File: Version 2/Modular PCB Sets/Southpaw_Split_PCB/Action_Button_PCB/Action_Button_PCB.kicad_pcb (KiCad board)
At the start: 2 copper layers, 133 x 112 mm, 28 parts, among them J1 Conn_01x06_Socket, J4 Conn_01x07_Socket, J5 Conn_01x07_Socket, X1 SW_SPST, Y1 SW_SPST

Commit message: general part layout
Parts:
- removed J4, J5: Conn_01x07_Socket, Connector_JST:JST_PH_B7B-PH-K_1x07_P2.00mm_Vertical
- removed R10, R11, R9: R, Resistor_THT:R_Axial_DIN0207_L6.3mm_D2.5mm_P10.16mm_Horizontal
- added J2: Conn_01x07_Socket, Connector_JST:JST_PH_B7B-PH-K_1x07_P2.00mm_Vertical, B.Cu at (176.0, 41.0)
- added J3: Conn_01x07_Socket, Connector_JST:JST_PH_B7B-PH-K_1x07_P2.00mm_Vertical, B.Cu at (63.0, 41.0)
- added R2: R, Resistor_THT:R_Axial_DIN0207_L6.3mm_D2.5mm_P10.16mm_Horizontal, F.Cu at (125.4, 83.0)
- added R3: R, Resistor_THT:R_Axial_DIN0207_L6.3mm_D2.5mm_P10.16mm_Horizontal, F.Cu at (97.8, 85.0)
- added R4: R, Resistor_THT:R_Axial_DIN0207_L6.3mm_D2.5mm_P10.16mm_Horizontal, F.Cu at (67.4, 93.0)
- moved D4 101.3 mm to (61.0, 92.0)
- moved D5 101.3 mm to (155.0, 53.0)
- moved D8 100.0 mm to (58.5, 56.0)
- moved R8 96.1 mm to (64.8, 57.0)
- moved D1 73.2 mm to (153.0, 87.0)
- moved D2 65.8 mm to (119.0, 82.0)
- moved R7 51.9 mm to (96.9, 49.0)
- moved D3 48.6 mm to (91.5, 84.0)
- moved R6 48.6 mm to (126.9, 46.0)
- moved D6 48.6 mm to (120.5, 45.0)
- moved R5 46.4 mm to (161.4, 53.0)
- moved D7 44.7 mm to (90.5, 48.0)
- moved J1 9.22 mm to (176.0, 105.0), turned to 90 degrees
- moved R1 1.08 mm to (158.9, 88.0)
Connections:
- D1 pad 1: RB -> A
- D2 pad 1: LB -> B
- D3 pad 1: Y -> RT
- D4 pad 1: X -> LT
- D5 pad 1: LT -> X
- D6 pad 1: RT -> Y
- D7 pad 1: B -> RB
- D8 pad 1: A -> LB
- R1 pad 1: Net-(D8-A) -> Net-(D1-A)
- R5 pad 1: Net-(D7-A) -> Net-(D5-A)
- R7 pad 1: Net-(D5-A) -> Net-(D7-A)
- R8 pad 1: Net-(D4-A) -> Net-(D8-A)
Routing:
- net /Gnd: track 351.0 -> 0.00 mm
- net /3V3: track 240.5 -> 0.00 mm
- net GND: track 238.2 -> 0.00 mm
- net 3v3: track 236.1 -> 0.00 mm
- net /Rotary_Encoder_DT: track 153.1 -> 0.00 mm, vias 2 -> 0
- net LB: track 149.7 -> 0.00 mm, vias 1 -> 0
- net /R3: track 147.1 -> 0.00 mm, vias 2 -> 0
- net /Rotary_Encoder_CLK: track 146.2 -> 0.00 mm, vias 1 -> 0
- net /L3: track 142.6 -> 0.00 mm, vias 2 -> 0
- net /Start: track 136.6 -> 0.00 mm, vias 2 -> 0
- net /Options: track 126.8 -> 0.00 mm, vias 1 -> 0
- net /Guide: track 121.0 -> 0.00 mm, vias 1 -> 0
- net /Right: track 111.6 -> 0.00 mm, vias 2 -> 0
- net RB: track 111.4 -> 0.00 mm
- net /SDA: track 110.3 -> 0.00 mm
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
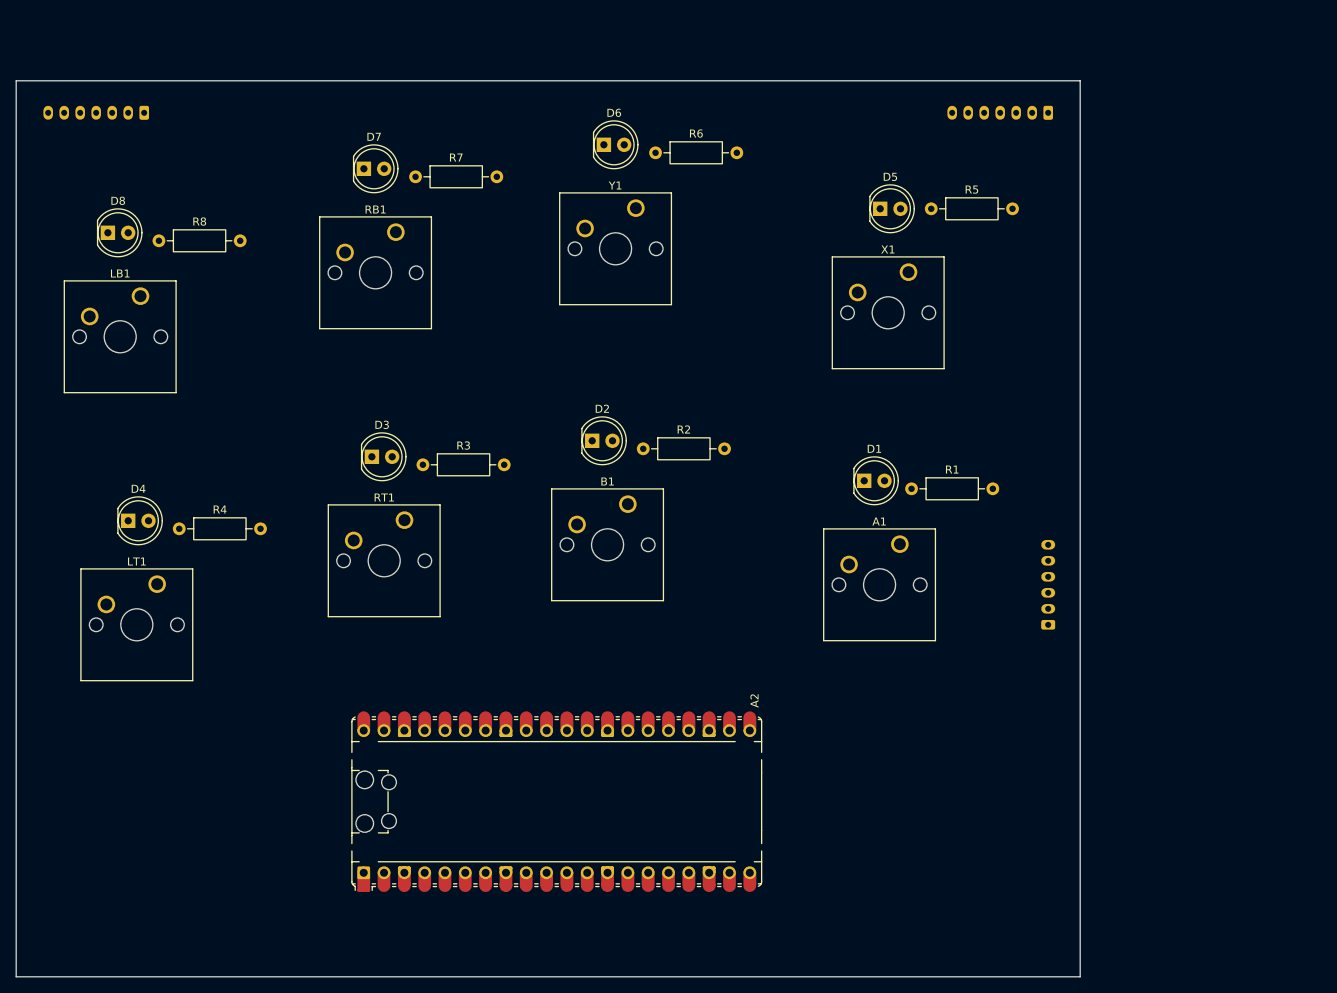
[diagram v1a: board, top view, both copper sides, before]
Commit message: First attempt to use solidworks sketches to align parts in kicad
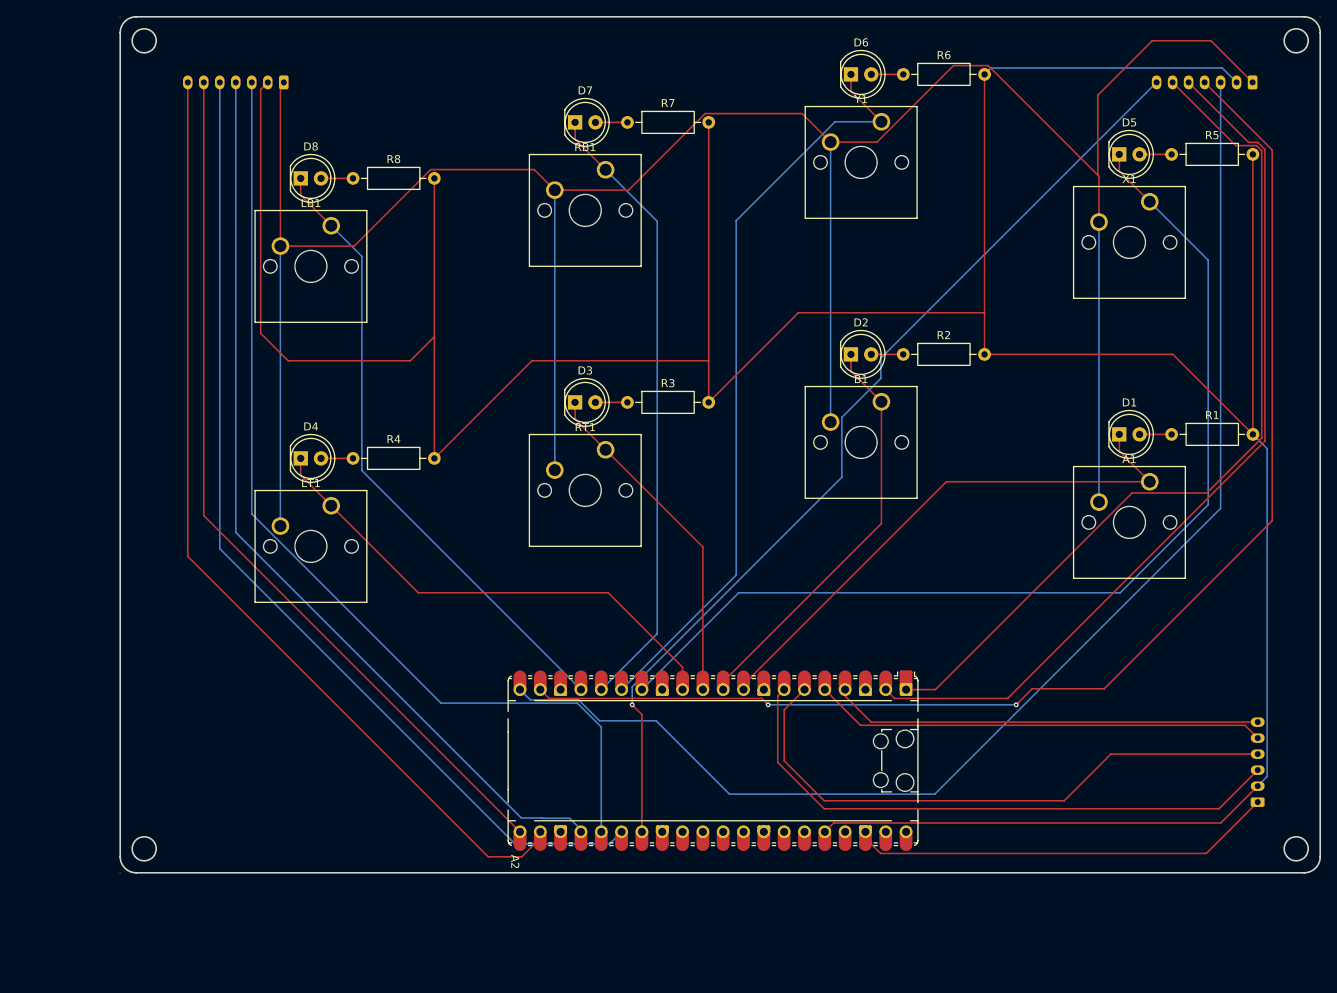
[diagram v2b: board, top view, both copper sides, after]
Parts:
- moved R2 34.6 mm to (157.9, 71.2)
- moved J1 34.3 mm to (202.2, 127.2)
- moved B1 34.2 mm to (155.2, 77.1)
- moved D2 34.1 mm to (151.3, 71.2)
- moved R1 33.2 mm to (191.4, 81.2)
- moved Y1 32.5 mm to (155.2, 42.1)
- moved R6 32.5 mm to (157.9, 36.2)
- moved D1 32.4 mm to (184.9, 81.2)
- moved A1 32.2 mm to (188.7, 87.1)
- moved D6 32.1 mm to (151.3, 36.2)
- moved X1 31.4 mm to (188.7, 52.1)
- moved R5 30.8 mm to (191.4, 46.2)
- moved D5 30.6 mm to (184.9, 46.2)
- moved RB1 27.4 mm to (120.7, 48.1)
- moved R7 27.3 mm to (123.4, 42.2)
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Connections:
- A2 pad 13: /Gnd -> GND
- A2 pad 18: /Gnd -> GND
- A2 pad 23: /Gnd -> GND
- A2 pad 28: /Gnd -> GND
- A2 pad 3: /Gnd -> GND
- A2 pad 36: /3V3 -> 3v3
- A2 pad 38: /Gnd -> GND
- A2 pad 8: /Gnd -> GND
- J1 pad 1: /Gnd -> GND
- J1 pad 2: /3V3 -> 3v3
- J2 pad 1: /Gnd -> GND
- J2 pad 2: /3V3 -> 3v3
- J3 pad 1: /Gnd -> GND
- J3 pad 2: /3V3 -> 3v3
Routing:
- net 3v3: track 0.00 -> 446.5 mm
- net GND: track 0.00 -> 376.4 mm
- net /SCK: track 0.00 -> 161.0 mm
- net /SDA: track 0.00 -> 160.1 mm, vias 0 -> 2
- net X: track 0.00 -> 128.8 mm
- net /Guide: track 0.00 -> 124.4 mm
- net /R3: track 0.00 -> 121.8 mm
- net /Encoder_Press: track 0.00 -> 121.3 mm, vias 0 -> 1
- net /Start: track 0.00 -> 120.6 mm
- net /L3: track 0.00 -> 115.1 mm
- net /Rotary_Encoder_DT: track 0.00 -> 110.6 mm
- net /Options: track 0.00 -> 110.1 mm
- net /Rotary_Encoder_CLK: track 0.00 -> 108.1 mm
- net Y: track 0.00 -> 95.3 mm
- net LB: track 0.00 -> 78.4 mm
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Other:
- board size 133 x 112 mm -> 150 x 107 mm

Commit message: finished movement pcb, need to make some small adjustments to action pcb
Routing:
- net GND: track 376.4 -> 469.0 mm
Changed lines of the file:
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@@
+	)
+	(segment
+		(start 205 40.65)
+		(end 205 124.35)
+		(width 0.2)
+		(layer "B.Cu")
+		(net 1)
+	)
+	(segment
+		(start 205 124.35)
+		(end 202.19 127.16)
+		(width 0.2)
+		(layer "B.Cu")
+		(net 1)
 	)
 	(segment
@@
 		(width 0.2)
 		(layer "B.Cu")
+		(net 1)
+	)
+	(segment
+		(start 201.55 37.2)
+		(end 205 40.65)
+		(width 0.2)
+		(layer "B.Cu")
